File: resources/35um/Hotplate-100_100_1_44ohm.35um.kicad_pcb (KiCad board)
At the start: 2 copper layers, 100 x 100 mm, 7 parts, among them J1 Hotplate_Power_Connection, J2 Hotplate_Power_Connection

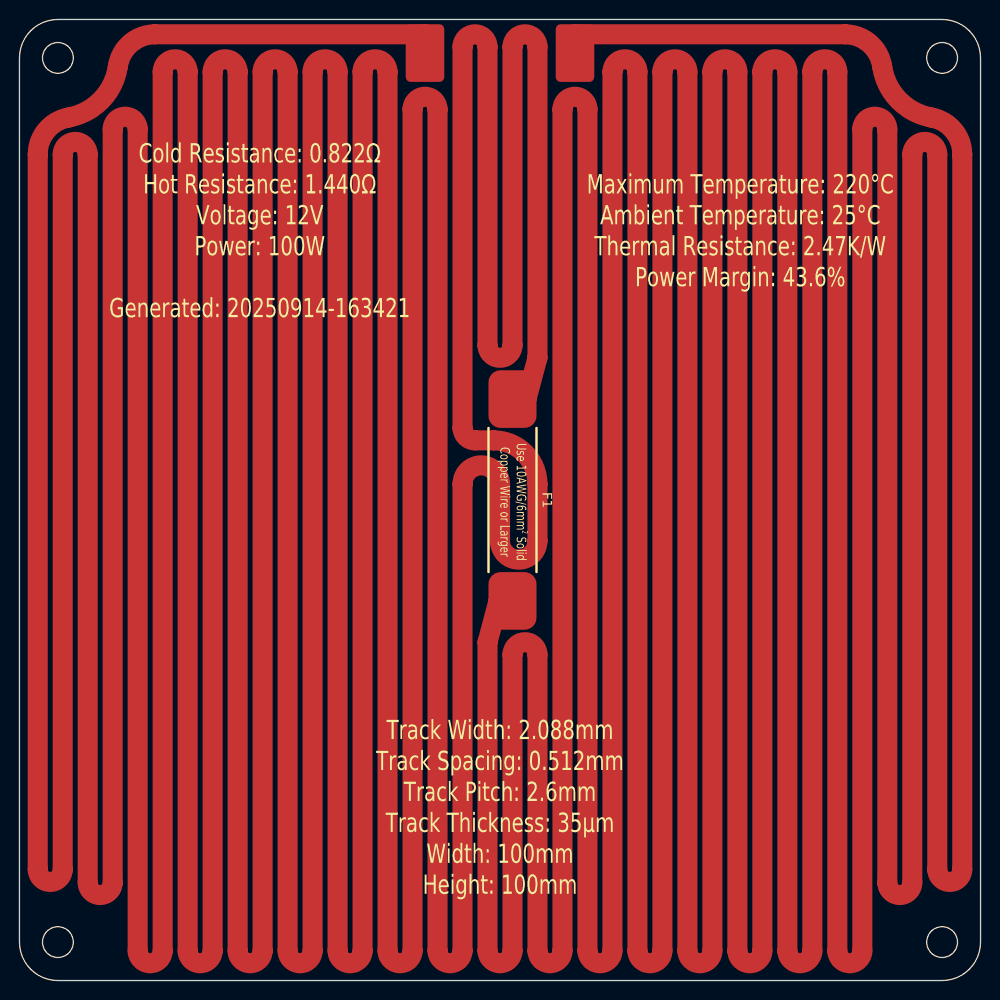
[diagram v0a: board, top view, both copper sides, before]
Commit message: Replaced obsolete 25mm thermal fuse footprint with new 35mm thermal fuse footprint.
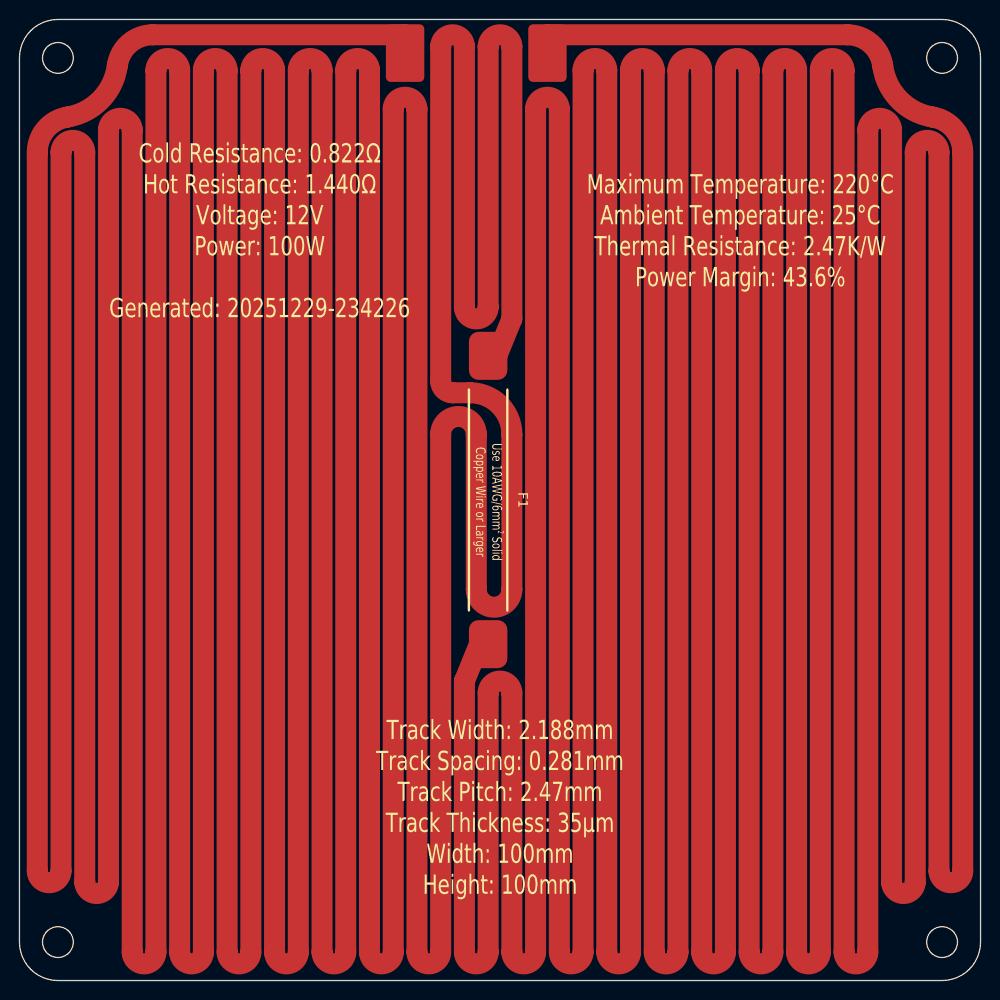
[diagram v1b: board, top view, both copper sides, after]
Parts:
- F1: footprint blg:Thermal Fuse, Front, 25mm -> blg:Thermal Fuse, SN100C, Front, 35mm
- moved J2 2.86 mm to (109.9, 58.5)
- moved F1 2.53 mm to (103.8, 105.0)
- moved J1 2.08 mm to (95.1, 58.5)
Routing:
- net Net-(J2-Pin_1): track 1696.2 -> 1877.1 mm
- net Net-(J1-Pin_1): track 1822.6 -> 1827.4 mm
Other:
- board text added: "Cold Resistance: 0.822Ω Hot Resistance: 1.440Ω Voltage: 12V Power: 100W Generated: 20251229-234226"
- board text added: "Track Width: 2.188mm Track Spacing: 0.281mm Track Pitch: 2.47mm Track Thickness: 35µm Width: 100mm Height: 100mm"
- board text removed: "Cold Resistance: 0.822Ω Hot Resistance: 1.440Ω Voltage: 12V Power: 100W Generated: 20250914-163421"
- board text removed: "Track Width: 2.088mm Track Spacing: 0.512mm Track Pitch: 2.6mm Track Thickness: 35µm Width: 100mm Height: 100mm"
